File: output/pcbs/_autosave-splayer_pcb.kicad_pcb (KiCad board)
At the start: 2 copper layers, 124.4 x 92.7 mm, 34 parts

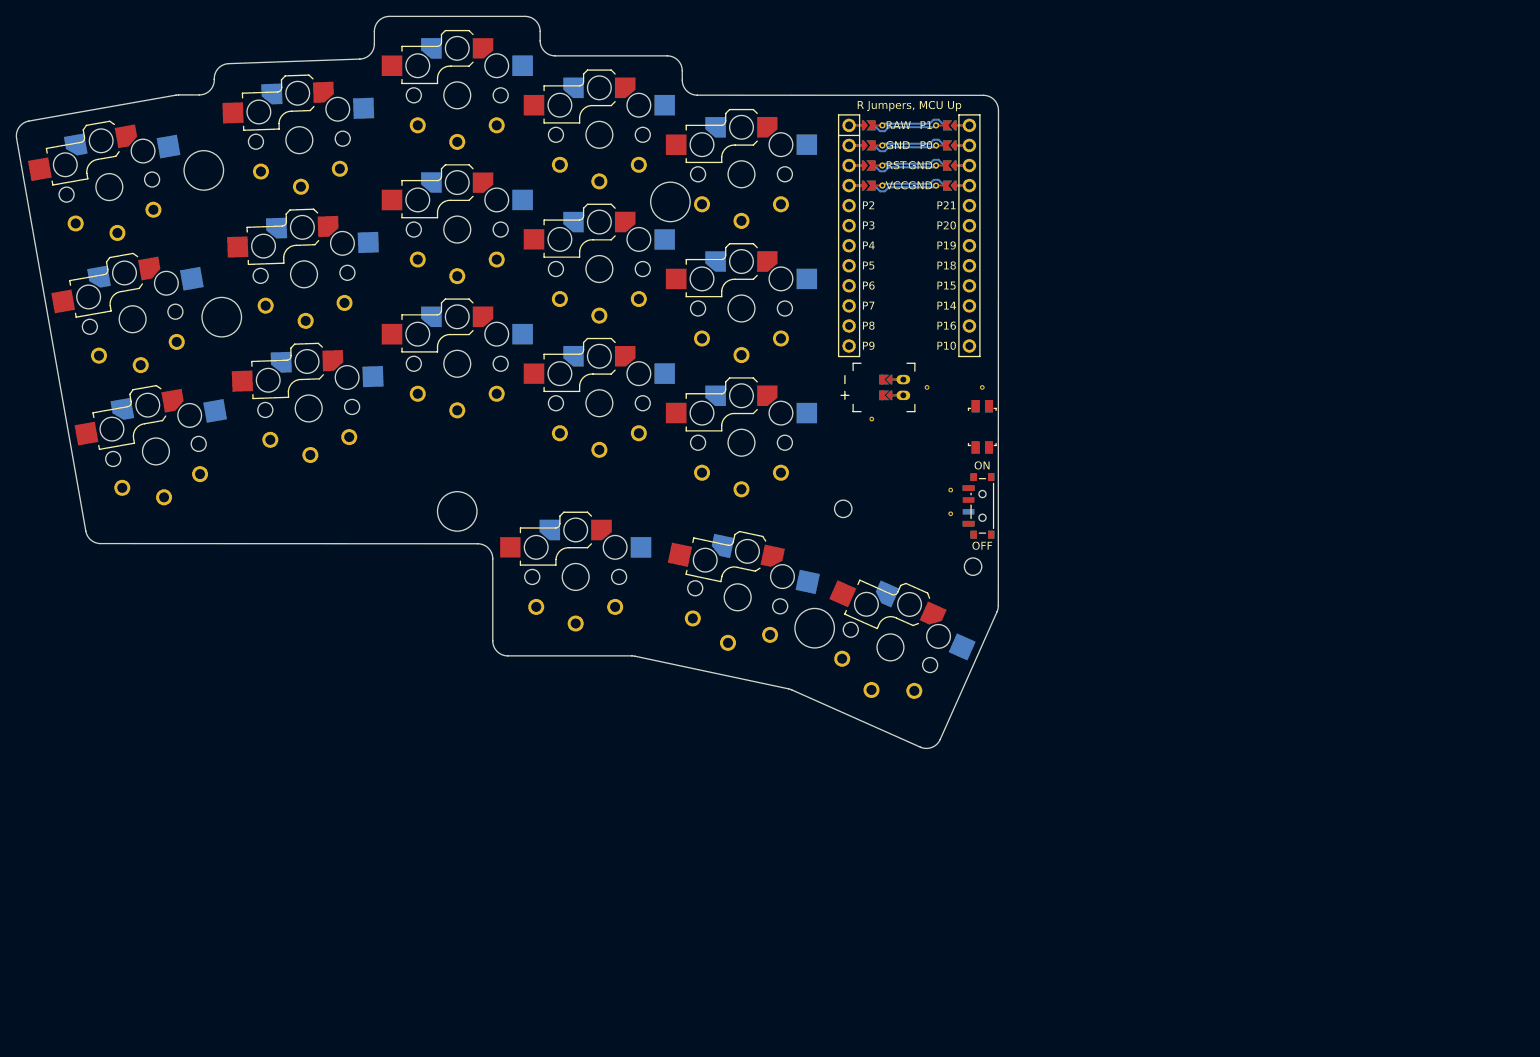
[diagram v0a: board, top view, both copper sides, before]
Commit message: redesigned the PCB to avoid errors, removed choc v2 support
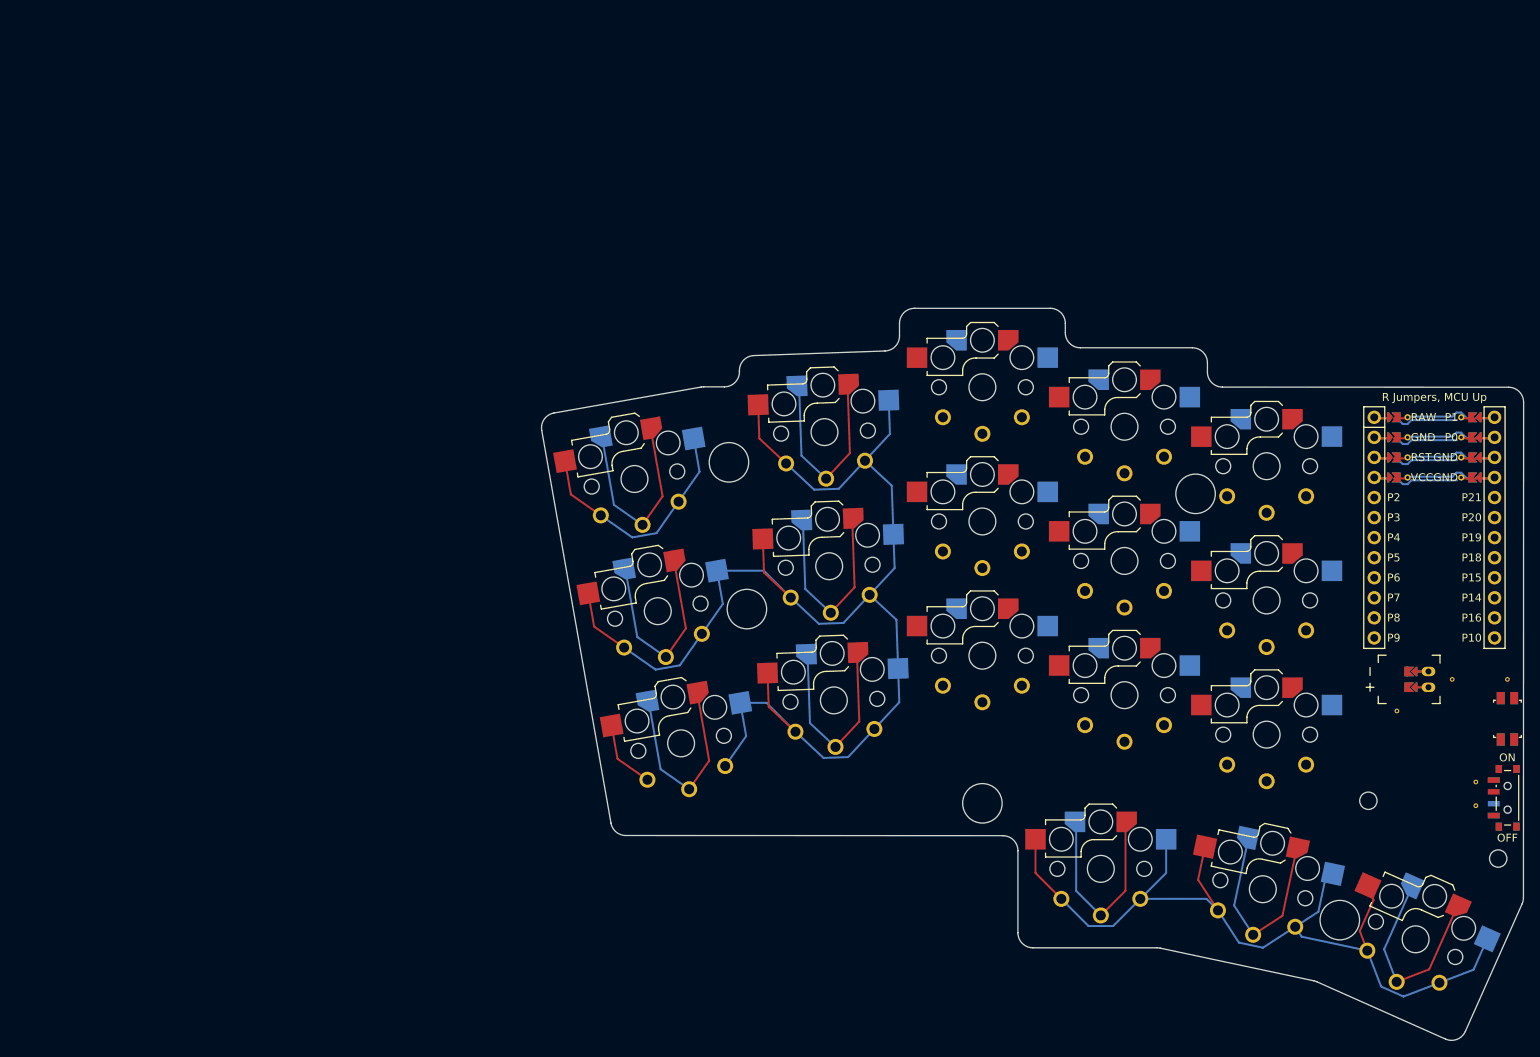
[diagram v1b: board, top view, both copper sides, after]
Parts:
- moved S6 76.1 mm to (184.7, 97.6)
- moved MH6 76.1 mm to (204.7, 144.6)
- moved REF** 76.1 mm to (267.2, 144.9)
- moved S14 76.1 mm to (240.7, 118.9)
- moved S2 76.1 mm to (163.6, 120.2)
- moved S12 76.1 mm to (222.7, 96.9)
- moved MH4 76.1 mm to (231.7, 105.4)
- moved RST1 76.1 mm to (271.2, 133.9)
- moved S18 76.1 mm to (259.5, 161.8)
- moved S8 76.1 mm to (204.7, 108.9)
- moved MH3 76.1 mm to (172.6, 101.4)
- moved REF** 76.1 mm to (257.2, 132.9)
- moved S3 76.1 mm to (160.6, 103.5)
- moved S15 76.1 mm to (240.7, 101.9)
- moved REF** 76.1 mm to (271.2, 128.9)
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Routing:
- net GND: track 30.6 -> 355.0 mm
- net P10: track 0.00 -> 26.4 mm
- net P8: track 0.00 -> 26.4 mm
- net P21: track 0.00 -> 26.4 mm
- net P14: track 0.00 -> 26.4 mm
- net P15: track 0.00 -> 26.4 mm
- net P0: track 9.83 -> 36.2 mm
- net P16: track 0.00 -> 26.4 mm
- net P18: track 0.00 -> 26.4 mm
- net P9: track 0.00 -> 26.4 mm
